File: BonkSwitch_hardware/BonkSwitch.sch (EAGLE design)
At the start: 95 parts, among them IC1 LMR16030SDDAR, IC2 LMR16006, IC3 FAN3227TMX, IC4 LMP8640, IC5 LMP8640, IC6 74LVC1G14DBV, Q1 SI2302, T1 IRF7493TRPBF, T2 IRF7493TRPBF, X1 XT60PW-M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

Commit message: More directory reorg
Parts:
- removed C12: 47uF 35V, rcl:C-EUC1210
- added C26: 120uF 35V, rcl:CPOL-EUE
- A2: OC_FARNELL (none) -> unknown
- C11: value 47uF 35V -> 22uF 35V
- IC2: value LMR16006 -> LMR16006XDDC; MF (none) -> TEXAS INSTRUMENTS; MPN (none) -> LMR16006XDDCR; OC_FARNELL unknown -> 3007251
- IC4, IC5: value LMP8640 -> LMP8640MK-T; MF (none) -> TEXAS INSTRUMENTS; MPN (none) -> LMP8640MK-T/NOPB; OC_FARNELL unknown -> 3005385; OC_RS (none) -> 824-7083
- Q1: MF (none) -> VISHAY; MPN (none) -> SI2302CDS-T1-GE3; OC_FARNELL (none) -> 1684049
- R1, R20: device rcl:R-EU_R0805 -> rcl:R-EU_R0603
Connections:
- net +24V: now also C26.+; no longer C12.1, LD4.A, LD5.A
- net +5V: now also LD4.A, LD5.A
- net GND: now also C26.-; no longer C12.2
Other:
- moved on the sheet: C11, LD1, R18, TP1

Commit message: Tuning Schematic.
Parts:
- A1, PCB1: MF (none) -> n/a; MPN (none) -> n/a
- A2: MF (none) -> FrSky; MPN (none) -> XM
- C11: value 22uF 35V -> 10uF 35V; MF (none) -> TAIYO YUDEN; MPN (none) -> GMK325AB7106MM-T; OC_FARNELL unknown -> 2309017; OC_RS (none) -> 766-1194
- C14: value 1uF -> 10nF
- C2, C3, C7, C8: value 3.3uF 100V -> 2.2uF 100V; MF (none) -> TDK; MPN (none) -> C3225X7R2A225K230AB; OC_FARNELL unknown -> 2112727; OC_RS (none) -> 766-1211
- C26: MF Panasonic -> PANASONIC
- C6: MF (none) -> TAIYO YUDEN; MPN (none) -> GMK325AB7106MM-T; OC_FARNELL unknown -> 2309017; OC_RS (none) -> 766-1194
- IC2: OC_RS (none) -> 914-2986
- L2: OC_RS (none) -> 789-6987
- Q1: value SI2302 -> SI2302CDS
- X1, X2, X3: MF (none) -> Amass
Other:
- note added: "SS is ~25mS"
- note removed: "SS is ~250mS"
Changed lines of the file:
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@@
 </part>
 <part name="GND22" library="supply1" deviceset="GND" device=""/>
-<part name="C2" library="rcl" deviceset="C-EU" device="C1210" value="3.3uF 100V">
-<attribute name="MF" value=""/>
-<attribute name="MPN" value=""/>
-<attribute name="OC_FARNELL" value="unknown"/>
-</part>
-<part name="C3" library="rcl" deviceset="C-EU" device="C1210" value="3.3uF 100V">
-<attribute name="MF" value=""/>
-<attribute name="MPN" value=""/>
-<attribute name="OC_FARNELL" value="unknown"/>
-</part>
-<part name="C11" library="rcl" deviceset="C-EU" device="C1210" value="22uF 35V">
-<attribute name="MF" value=""/>
-<attribute name="MPN" value=""/>
-<attribute name="OC_FARNELL" value="unknown"/>
+<part name="C2" library="rcl" deviceset="C-EU" device="C1210" value="2.2uF 100V">
+<attribute name="MF" value="TDK"/>
+<attribute name="MPN" value="C3225X7R2A225K230AB"/>
+<attribute name="OC_FARNELL" value="2112727"/>
+<attribute name="OC_RS" value="766-1211"/>
+</part>
+<part name="C3" library="rcl" deviceset="C-EU" device="C1210" value="2.2uF 100V">
+<attribute name="MF" value="TDK"/>
+<attribute name="MPN" value="C3225X7R2A225K230AB"/>
+<attribute name="OC_FARNELL" value="2112727"/>
+<attribute name="OC_RS" value="766-1211"/>
+</part>
+<part name="C11" library="rcl" deviceset="C-EU" device="C1210" value="10uF 35V">
+<attribute name="MF" value="TAIYO YUDEN"/>
+<attribute name="MPN" value="GMK325AB7106MM-T"/>
+<attribute name="OC_FARNELL" value="2309017"/>
+<attribute name="OC_RS" value="766-1194"/>
 </part>
 <part name="GND23" library="supply1" deviceset="GND" device=""/>
@@
 </part>
 <part name="GND30" library="supply1" deviceset="GND" device=""/>
-<part name="C14" library="rcl" deviceset="C-EU" device="C0603" value="1uF">
+<part name="C14" library="rcl" deviceset="C-EU" device="C0603" value="10nF">
 <attribute name="MF" value=""/>
 <attribute name="MPN" value=""/>
@@
 <part name="P+8" library="supply1" deviceset="VCC" device=""/>
 <part name="X1" library="con-amass" deviceset="XT60" device="PW-M">
-<attribute name="MF" value=""/>
+<attribute name="MF" value="Amass"/>
 <attribute name="MPN" value=""/>
 <attribute name="OC_FARNELL" value="unknown"/>
@@
 <part name="GND8" library="supply1" deviceset="GND" device=""/>
 <part name="PCB1" library="dp_devices" deviceset="PCB_DP_RECTANGLE" device="-100X62">
-<attribute name="MF" value=""/>
-<attribute name="MPN" value=""/>
+<attribute name="MF" value="n/a"/>
+<attribute name="MPN" value="n/a"/>
 <attribute name="OC_FARNELL" value="unknown"/>
 </part>
@@
 <attribute name="MPN" value="LMR16006XDDCR"/>
 <attribute name="OC_FARNELL" value="3007251"/>
+<attribute name="OC_RS" value="914-2986"/>
 </part>
 <part name="R5" library="rcl" deviceset="R-EU_" device="R0603" value="82k">
@@
 </part>
 <part name="C6" library="rcl" deviceset="C-EU" device="C1210" value="10uF 35V">
-<attribute name="MF" value=""/>
-<attribute name="MPN" value=""/>
-<attribute name="OC_FARNELL" value="unknown"/>
+<attribute name="MF" value="TAIYO YUDEN"/>
+<attribute name="MPN" value="GMK325AB7106MM-T"/>
+<attribute name="OC_FARNELL" value="2309017"/>
+<attribute name="OC_RS" value="766-1194"/>
 </part>
 <part name="R22" library="rcl" deviceset="R-EU_" device="R0603" value="68k">
@@
 <attribute name="MPN" value="7447714470"/>
 <attribute name="OC_FARNELL" value="2082682"/>
+<attribute name="OC_RS" value="789-6987"/>
 </part>
 <part name="GND18" library="supply1" deviceset="GND" device=""/>
-<part name="C7" library="rcl" deviceset="C-EU" device="C1210" value="3.3uF 100V">
-<attribute name="MF" value=""/>
-<attribute name="MPN" value=""/>
-<attribute name="OC_FARNELL" value="unknown"/>
-</part>
-<part name="C8" library="rcl" deviceset="C-EU" device="C1210" value="3.3uF 100V">
-<attribute name="MF" value=""/>
-<attribute name="MPN" value=""/>
-<attribute name="OC_FARNELL" value="unknown"/>
+<part name="C7" library="rcl" deviceset="C-EU" device="C1210" value="2.2uF 100V">
+<attribute name="MF" value="TDK"/>
+<attribute name="MPN" value="C3225X7R2A225K230AB"/>
+<attribute name="OC_FARNELL" value="2112727"/>
+<attribute name="OC_RS" value="766-1211"/>
+</part>
+<part name="C8" library="rcl" deviceset="C-EU" device="C1210" value="2.2uF 100V">
+<attribute name="MF" value="TDK"/>
+<attribute name="MPN" value="C3225X7R2A225K230AB"/>
+<attribute name="OC_FARNELL" value="2112727"/>
+<attribute name="OC_RS" value="766-1211"/>
 </part>
 <part name="GND20" library="supply1" deviceset="GND" device=""/>
@@
 <part name="GND40" library="supply1" deviceset="GND" device=""/>
 <part name="X2" library="con-amass" deviceset="XT30" device="PW-F">
-<attribute name="MF" value=""/>
+<attribute name="MF" value="Amass"/>
 <attribute name="MPN" value=""/>
 <attribute name="OC_FARNELL" value="unknown"/>
 </part>
 <part name="X3" library="con-amass" deviceset="XT30" device="PW-F">
-<attribute name="MF" value=""/>
+<attribute name="MF" value="Amass"/>
 <attribute name="MPN" value=""/>
 <attribute name="OC_FARNELL" value="unknown"/>
@@
 </part>
 <part name="A1" library="ThingySticks" deviceset="FEATHERWING" device="_NODIM">
-<attribute name="MF" value=""/>
-<attribute name="MPN" value=""/>
+<attribute name="MF" value="n/a"/>
+<attribute name="MPN" value="n/a"/>
 <attribute name="OC_FARNELL" value="unknown"/>
 </part>
@@
 </part>
 <part name="GND49" library="supply1" deviceset="GND" device=""/>
-<part name="Q1" library="transistor-fet" deviceset="SI2302" device="">
+<part name="Q1" library="transistor-fet" deviceset="SI2302" device="" value="SI2302CDS">
 <attribute name="MF" value="VISHAY"/>
 <attribute name="MPN" value="SI2302CDS-T1-GE3"/>
@@
 <part name="+3V5" library="supply1" deviceset="+3V3" device=""/>
 <part name="A2" library="general" deviceset="FRSKY_XM+" device="">
-<attribute name="MF" value=""/>
-<attribute name="MPN" value=""/>
+<attribute name="MF" value="FrSky"/>
+<attribute name="MPN" value="XM"/>
 <attribute name="OC_FARNELL" value="unknown"/>
 </part>
@@
 <part name="P+16" library="supply1" deviceset="+5V" device=""/>
 <part name="C26" library="rcl" deviceset="CPOL-EU" device="E" value="120uF 35V">
-<attribute name="MF" value="Panasonic"/>
+<attribute name="MF" value="PANASONIC"/>
 <attribute name="MPN" value="35SVPF120M"/>
 <attribute name="OC_FARNELL" value="2354806"/>
@@
 <text x="330.2" y="147.32" size="1.778" layer="97" align="center-left">X</text>
 <text x="330.2" y="73.66" size="1.778" layer="97" align="center-left">X</text>
-<text x="238.76" y="198.12" size="1.778" layer="97">SS is ~250mS</text>
+<text x="238.76" y="198.12" size="1.778" layer="97">SS is ~25mS</text>
 <text x="167.64" y="25.4" size="1.778" layer="97" align="center-left">X</text>
 <text x="167.64" y="27.94" size="1.778" layer="97" align="center-left">X</text>
@@
 <attribute name="MF" x="187.96" y="231.14" size="1.778" layer="96" display="off"/>
 <attribute name="MPN" x="187.96" y="231.14" size="1.778" layer="96" display="off"/>
+<attribute name="OC_RS" x="187.96" y="231.14" size="1.778" layer="96" rot="MR0" display="off"/>
 </instance>
 <instance part="C3" gate="G$1" x="195.58" y="223.52" rot="MR0">
@@
 <attribute name="MF" x="195.58" y="223.52" size="1.778" layer="96" display="off"/>
 <attribute name="MPN" x="195.58" y="223.52" size="1.778" layer="96" display="off"/>
+<attribute name="OC_RS" x="195.58" y="223.52" size="1.778" layer="96" rot="MR0" display="off"/>
 </instance>
 <instance part="C11" gate="G$1" x="342.9" y="210.82">
@@
 <attribute name="MF" x="342.9" y="210.82" size="1.778" layer="96" display="off"/>
 <attribute name="MPN" x="342.9" y="210.82" size="1.778" layer="96" display="off"/>
+<attribute name="OC_RS" x="342.9" y="210.82" size="1.778" layer="96" display="off"/>
 </instance>
 <instance part="GND23" gate="1" x="195.58" y="203.2"/>
@@
 <attribute name="MF" x="175.26" y="116.84" size="1.778" layer="96" display="off"/>
 <attribute name="MPN" x="175.26" y="116.84" size="1.778" layer="96" display="off"/>
+<attribute name="OC_RS" x="175.26" y="116.84" size="1.778" layer="96" display="off"/>
 </instance>
 <instance part="R5" gate="G$1" x="152.4" y="114.3" rot="R90">
@@
 <attribute name="MF" x="231.14" y="101.6" size="1.778" layer="96" display="off"/>
 <attribute name="MPN" x="231.14" y="101.6" size="1.778" layer="96" display="off"/>
+<attribute name="OC_RS" x="231.14" y="101.6" size="1.778" layer="96" display="off"/>
 </instance>
 <instance part="R22" gate="G$1" x="223.52" y="109.22" rot="R90">
@@
 <attribute name="MF" x="210.82" y="116.84" size="1.778" layer="96" display="off"/>
 <attribute name="MPN" x="210.82" y="116.84" size="1.778" layer="96" display="off"/>
+<attribute name="OC_RS" x="210.82" y="116.84" size="1.778" layer="96" display="off"/>
 </instance>
 <instance part="GND18" gate="1" x="198.12" y="83.82"/>
@@
 <attribute name="MF" x="137.16" y="111.76" size="1.778" layer="96" display="off"/>
 <attribute name="MPN" x="137.16" y="111.76" size="1.778" layer="96" display="off"/>
+<attribute name="OC_RS" x="137.16" y="111.76" size="1.778" layer="96" rot="MR0" display="off"/>
 </instance>
 <instance part="C8" gate="G$1" x="144.78" y="101.6" rot="MR0">
@@
 <attribute name="MF" x="144.78" y="101.6" size="1.778" layer="96" display="off"/>
 <attribute name="MPN" x="144.78" y="101.6" size="1.778" layer="96" display="off"/>
+<attribute name="OC_RS" x="144.78" y="101.6" size="1.778" layer="96" rot="MR0" display="off"/>
 </instance>
 <instance part="GND20" gate="1" x="144.78" y="88.9"/>

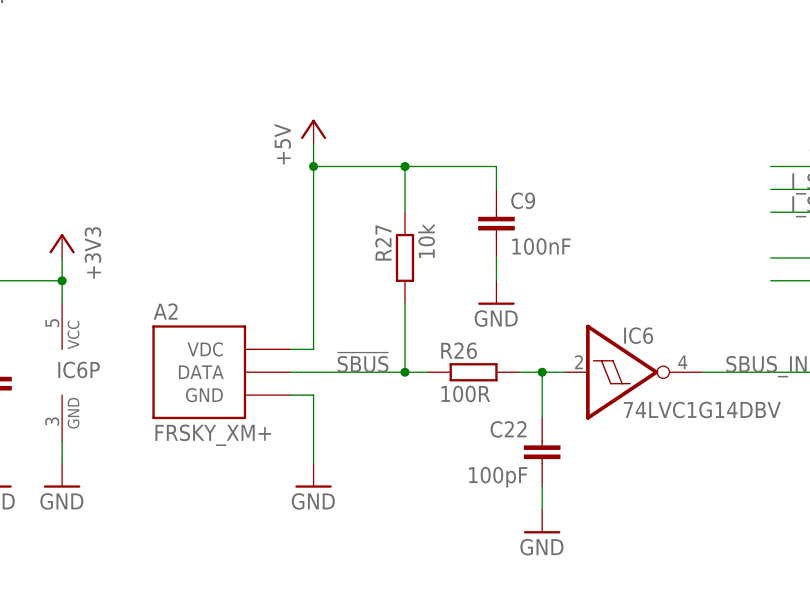
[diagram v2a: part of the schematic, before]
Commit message: Fixed SBUS bias resistor.
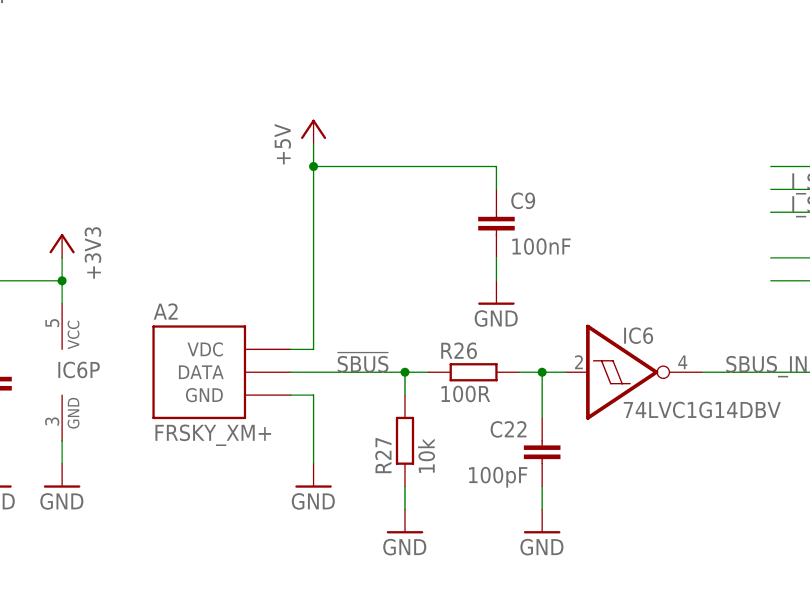
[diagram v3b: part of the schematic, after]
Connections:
- net +5V: no longer R27.1
- net GND: now also R27.1
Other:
- moved on the sheet: R27
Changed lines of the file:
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@@
 </part>
 <part name="GND55" library="supply1" deviceset="GND" device=""/>
+<part name="GND25" library="supply1" deviceset="GND" device=""/>
 </parts>
 <sheets>
@@
 <instance part="GND36" gate="1" x="25.4" y="17.78"/>
 <instance part="GND48" gate="1" x="17.78" y="17.78"/>
-<instance part="R27" gate="G$1" x="63.5" y="43.18" rot="MR270">
-<attribute name="OC_FARNELL" x="63.5" y="43.18" size="1.778" layer="96" display="off"/>
-<attribute name="MF" x="63.5" y="43.18" size="1.778" layer="96" display="off"/>
-<attribute name="MPN" x="63.5" y="43.18" size="1.778" layer="96" display="off"/>
+<instance part="R27" gate="G$1" x="63.5" y="22.86" rot="R90">
+<attribute name="OC_FARNELL" x="63.5" y="22.86" size="1.778" layer="96" rot="MR180" display="off"/>
+<attribute name="MF" x="63.5" y="22.86" size="1.778" layer="96" rot="MR180" display="off"/>
+<attribute name="MPN" x="63.5" y="22.86" size="1.778" layer="96" rot="MR180" display="off"/>
 </instance>
 <instance part="C22" gate="G$1" x="78.74" y="22.86" rot="MR0">
@@
 </instance>
 <instance part="GND55" gate="1" x="335.28" y="195.58"/>
+<instance part="GND25" gate="1" x="63.5" y="12.7"/>
 </instances>
 <busses>
@@
 <wire x1="335.28" y1="215.9" x2="335.28" y2="198.12" width="0.1524" layer="91"/>
 <pinref part="GND55" gate="1" pin="GND"/>
+</segment>
+<segment>
+<pinref part="GND25" gate="1" pin="GND"/>
+<wire x1="63.5" y1="17.78" x2="63.5" y2="15.24" width="0.1524" layer="91"/>
+<pinref part="R27" gate="G$1" pin="1"/>
 </segment>
 </net>
@@
 <wire x1="53.34" y1="53.34" x2="53.34" y2="55.88" width="0.1524" layer="91"/>
 <wire x1="73.66" y1="50.8" x2="73.66" y2="53.34" width="0.1524" layer="91"/>
-<wire x1="73.66" y1="53.34" x2="63.5" y2="53.34" width="0.1524" layer="91"/>
 <junction x="53.34" y="53.34"/>
 <pinref part="P+12" gate="1" pin="+5V"/>
-<pinref part="R27" gate="G$1" pin="1"/>
-<wire x1="63.5" y1="53.34" x2="53.34" y2="53.34" width="0.1524" layer="91"/>
-<wire x1="63.5" y1="48.26" x2="63.5" y2="53.34" width="0.1524" layer="91"/>
-<junction x="63.5" y="53.34"/>
+<wire x1="73.66" y1="53.34" x2="53.34" y2="53.34" width="0.1524" layer="91"/>
 <pinref part="A2" gate="G$1" pin="VDC"/>
 </segment>
@@
 <pinref part="R27" gate="G$1" pin="2"/>
 <wire x1="63.5" y1="30.48" x2="66.04" y2="30.48" width="0.1524" layer="91"/>
-<wire x1="63.5" y1="38.1" x2="63.5" y2="30.48" width="0.1524" layer="91"/>
+<wire x1="63.5" y1="27.94" x2="63.5" y2="30.48" width="0.1524" layer="91"/>
 <junction x="63.5" y="30.48"/>
 <pinref part="A2" gate="G$1" pin="DATA"/>

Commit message: Moved +5V rail monitoring to A4
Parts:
- added R7: 33k, rcl:R-EU_R0603
- R28: value 100k -> 47k
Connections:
- removed net N$5: A1.GPIOA4
- net 5V_MON: now also A1.GPIOA4, R7.2; no longer A1.GPIO9
- net GND: now also R7.1
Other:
- note added: "+8.0V max 5V_MON * 2.4242 = +5V"
- note removed: "+6.6V max 5V_MON * 2 = +5V"
- moved on the sheet: C10
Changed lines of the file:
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@@
 </part>
 <part name="GND35" library="supply1" deviceset="GND" device=""/>
-<part name="R28" library="rcl" deviceset="R-EU_" device="R0603" value="100k">
+<part name="R28" library="rcl" deviceset="R-EU_" device="R0603" value="47k">
 <attribute name="MF" value=""/>
 <attribute name="MPN" value=""/>
@@
 <part name="GND55" library="supply1" deviceset="GND" device=""/>
 <part name="GND25" library="supply1" deviceset="GND" device=""/>
+<part name="R7" library="rcl" deviceset="R-EU_" device="R0603" value="33k">
+<attribute name="MF" value=""/>
+<attribute name="MPN" value=""/>
+<attribute name="OC_FARNELL" value="unknown"/>
+</part>
+<part name="GND56" library="supply1" deviceset="GND" device=""/>
 </parts>
 <sheets>
@@
 <text x="124.46" y="35.56" size="1.778" layer="97" rot="MR0" align="center-left">X</text>
 <text x="124.46" y="38.1" size="1.778" layer="97" rot="MR0" align="center-left">X</text>
-<text x="20.32" y="86.36" size="1.778" layer="97">+6.6V max
-5V_MON * 2 = +5V</text>
+<text x="20.32" y="86.36" size="1.778" layer="97">+8.0V max
+5V_MON * 2.4242 = +5V</text>
 </plain>
 <instances>
@@
 <attribute name="MPN" x="12.7" y="88.9" size="1.778" layer="96" display="off"/>
 </instance>
-<instance part="C10" gate="G$1" x="12.7" y="76.2">
-<attribute name="OC_FARNELL" x="12.7" y="76.2" size="1.778" layer="96" display="off"/>
-<attribute name="MF" x="12.7" y="76.2" size="1.778" layer="96" display="off"/>
-<attribute name="MPN" x="12.7" y="76.2" size="1.778" layer="96" display="off"/>
-</instance>
-<instance part="GND37" gate="1" x="12.7" y="63.5"/>
+<instance part="C10" gate="G$1" x="20.32" y="76.2">
+<attribute name="OC_FARNELL" x="20.32" y="76.2" size="1.778" layer="96" display="off"/>
+<attribute name="MF" x="20.32" y="76.2" size="1.778" layer="96" display="off"/>
+<attribute name="MPN" x="20.32" y="76.2" size="1.778" layer="96" display="off"/>
+</instance>
+<instance part="GND37" gate="1" x="20.32" y="63.5"/>
 <instance part="P+13" gate="1" x="12.7" y="99.06" rot="MR0"/>
 <instance part="T1" gate="G$1" x="345.44" y="121.92">
@@
 <instance part="GND55" gate="1" x="335.28" y="195.58"/>
 <instance part="GND25" gate="1" x="63.5" y="12.7"/>
+<instance part="R7" gate="G$1" x="12.7" y="73.66" rot="R90">
+<attribute name="OC_FARNELL" x="12.7" y="73.66" size="1.778" layer="96" display="off"/>
+<attribute name="MF" x="12.7" y="73.66" size="1.778" layer="96" display="off"/>
+<attribute name="MPN" x="12.7" y="73.66" size="1.778" layer="96" display="off"/>
+</instance>
+<instance part="GND56" gate="1" x="12.7" y="63.5"/>
 </instances>
 <busses>
@@
 <pinref part="C10" gate="G$1" pin="2"/>
 <pinref part="GND37" gate="1" pin="GND"/>
-<wire x1="12.7" y1="71.12" x2="12.7" y2="66.04" width="0.1524" layer="91"/>
+<wire x1="20.32" y1="71.12" x2="20.32" y2="66.04" width="0.1524" layer="91"/>
 </segment>
 <segment>
@@
 <wire x1="63.5" y1="17.78" x2="63.5" y2="15.24" width="0.1524" layer="91"/>
 <pinref part="R27" gate="G$1" pin="1"/>
+</segment>
+<segment>
+<pinref part="GND56" gate="1" pin="GND"/>
+<pinref part="R7" gate="G$1" pin="1"/>
+<wire x1="12.7" y1="66.04" x2="12.7" y2="68.58" width="0.1524" layer="91"/>
 </segment>
 </net>
@@
 <net name="5V_MON" class="0">
 <segment>
-<wire x1="167.64" y1="35.56" x2="185.42" y2="35.56" width="0.1524" layer="91"/>
-<label x="170.18" y="35.56" size="1.778" layer="95"/>
-<pinref part="A1" gate="G$1" pin="GPIO9"/>
-</segment>
-<segment>
 <pinref part="R28" gate="G$1" pin="1"/>
 <wire x1="12.7" y1="83.82" x2="12.7" y2="81.28" width="0.1524" layer="91"/>
+<wire x1="12.7" y1="81.28" x2="20.32" y2="81.28" width="0.1524" layer="91"/>
 <pinref part="C10" gate="G$1" pin="1"/>
-<wire x1="12.7" y1="81.28" x2="30.48" y2="81.28" width="0.1524" layer="91"/>
+<wire x1="20.32" y1="81.28" x2="38.1" y2="81.28" width="0.1524" layer="91"/>
+<wire x1="20.32" y1="78.74" x2="20.32" y2="81.28" width="0.1524" layer="91"/>
+<junction x="20.32" y="81.28"/>
+<label x="30.48" y="81.28" size="1.778" layer="95"/>
+<pinref part="R7" gate="G$1" pin="2"/>
 <wire x1="12.7" y1="78.74" x2="12.7" y2="81.28" width="0.1524" layer="91"/>
 <junction x="12.7" y="81.28"/>
-<label x="22.86" y="81.28" size="1.778" layer="95"/>
+</segment>
+<segment>
+<pinref part="A1" gate="G$1" pin="GPIOA4"/>
+<wire x1="124.46" y1="43.18" x2="104.14" y2="43.18" width="0.1524" layer="91"/>
+<label x="119.38" y="43.18" size="1.778" layer="95" rot="MR0"/>
 </segment>
 </net>
@@
 </segment>
 </net>
-<net name="N$5" class="0">
-<segment>
-<pinref part="A1" gate="G$1" pin="GPIOA4"/>
-<wire x1="124.46" y1="43.18" x2="104.14" y2="43.18" width="0.1524" layer="91"/>
-</segment>
-</net>

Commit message: Updated schematic & BoM
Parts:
- A1, PCB1: MF n/a -> (none); MPN n/a -> (none)
- A2: MF FrSky -> (none); MPN XM -> (none)
- X1, X2, X3: MF Amass -> (none)
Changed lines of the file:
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@@
 <part name="P+8" library="supply1" deviceset="VCC" device=""/>
 <part name="X1" library="con-amass" deviceset="XT60" device="PW-M">
-<attribute name="MF" value="Amass"/>
+<attribute name="MF" value=""/>
 <attribute name="MPN" value=""/>
 <attribute name="OC_FARNELL" value="unknown"/>
@@
 <part name="GND8" library="supply1" deviceset="GND" device=""/>
 <part name="PCB1" library="dp_devices" deviceset="PCB_DP_RECTANGLE" device="-100X62">
-<attribute name="MF" value="n/a"/>
-<attribute name="MPN" value="n/a"/>
+<attribute name="MF" value=""/>
+<attribute name="MPN" value=""/>
 <attribute name="OC_FARNELL" value="unknown"/>
 </part>
@@
 <part name="GND40" library="supply1" deviceset="GND" device=""/>
 <part name="X2" library="con-amass" deviceset="XT30" device="PW-F">
-<attribute name="MF" value="Amass"/>
+<attribute name="MF" value=""/>
 <attribute name="MPN" value=""/>
 <attribute name="OC_FARNELL" value="unknown"/>
 </part>
 <part name="X3" library="con-amass" deviceset="XT30" device="PW-F">
-<attribute name="MF" value="Amass"/>
+<attribute name="MF" value=""/>
 <attribute name="MPN" value=""/>
 <attribute name="OC_FARNELL" value="unknown"/>
@@
 </part>
 <part name="A1" library="ThingySticks" deviceset="FEATHERWING" device="_NODIM">
-<attribute name="MF" value="n/a"/>
-<attribute name="MPN" value="n/a"/>
+<attribute name="MF" value=""/>
+<attribute name="MPN" value=""/>
 <attribute name="OC_FARNELL" value="unknown"/>
 </part>
@@
 <part name="+3V5" library="supply1" deviceset="+3V3" device=""/>
 <part name="A2" library="general" deviceset="FRSKY_XM+" device="">
-<attribute name="MF" value="FrSky"/>
-<attribute name="MPN" value="XM"/>
-<attribute name="OC_FARNELL" value="unknown"/>
-</part>
+<attribute name="MF" value=""/>
+<attribute name="MPN" value=""/>
+<attribute name="OC_FARNELL" value="unknown"/>
+</part>
